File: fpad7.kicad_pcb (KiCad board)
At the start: 2 copper layers, 100 x 100 mm, 73 parts, among them J2 Conn_01x12, SW1 SW_Push, SW10 SW_Push, SW11 SW_Push, SW12 SW_Push, SW13 SW_Push, SW14 SW_Push, SW15 SW_Push, SW16 SW_Push, SW17 SW_Push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

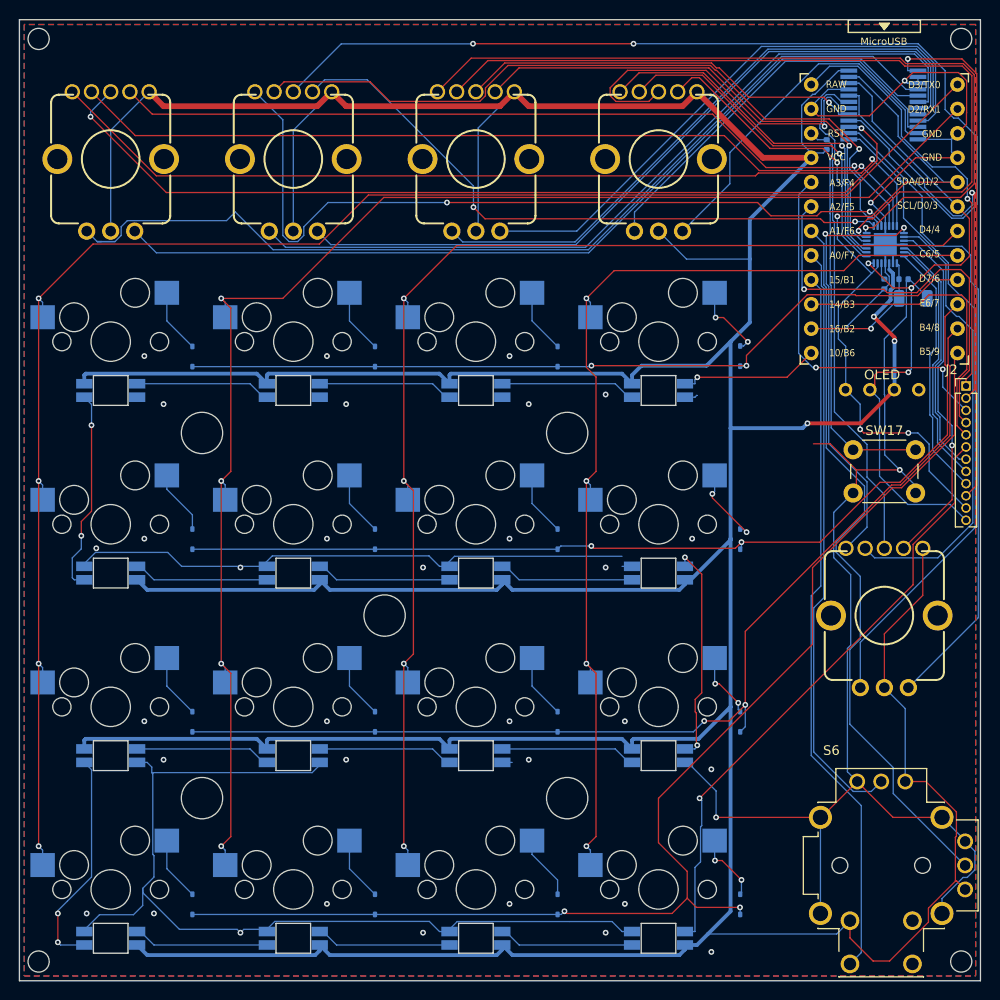
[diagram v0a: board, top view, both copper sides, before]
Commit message: update: errata for rev1
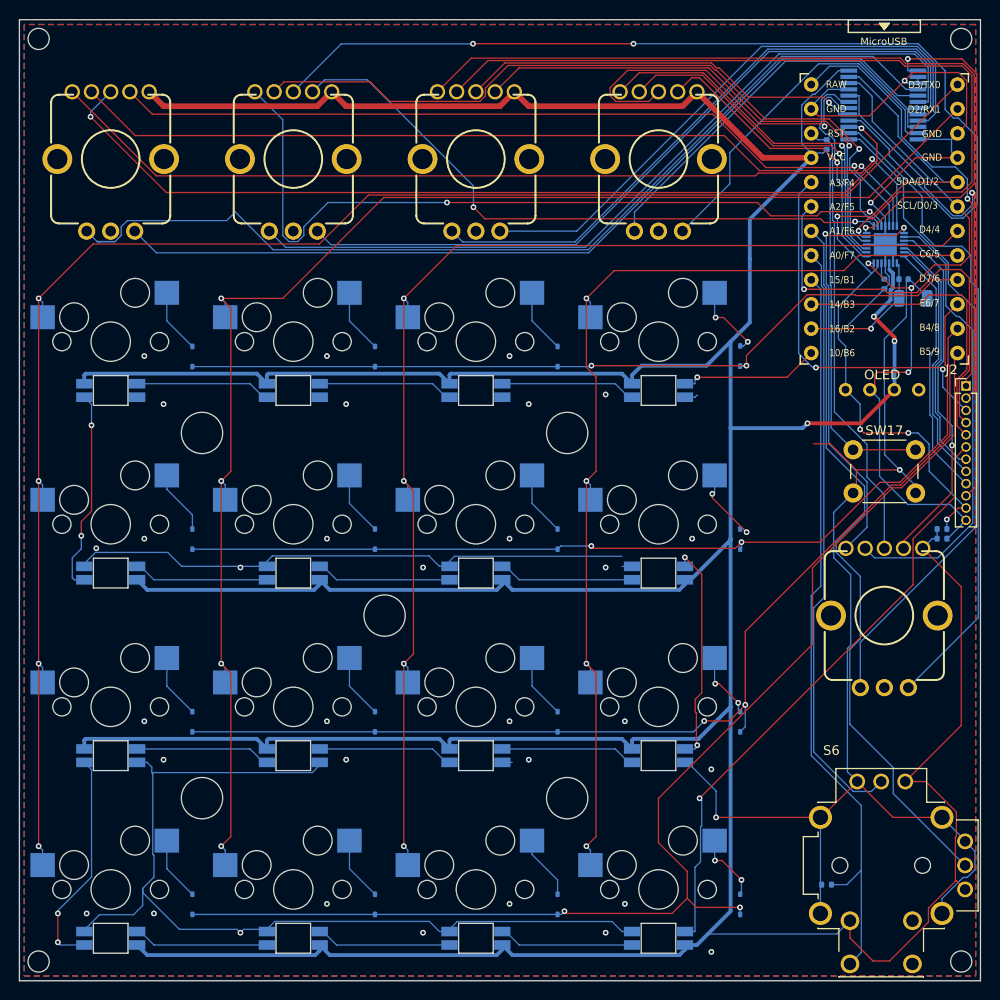
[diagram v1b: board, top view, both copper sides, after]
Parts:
- added R4: 10k, Resistor_SMD:R_0402_1005Metric, B.Cu at (104.0, 110.0)
- added R5: 3k3, Resistor_SMD:R_0402_1005Metric, B.Cu at (116.0, 73.0)
- added R6: 3k3, Resistor_SMD:R_0402_1005Metric, B.Cu at (116.0, 74.0)
- R1: value 7.6k -> 7.5k
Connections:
- S1 pad C: VCC -> GND
- S2 pad C: VCC -> GND
- S3 pad C: VCC -> GND
- S4 pad C: VCC -> GND
- S5 pad C: VCC -> GND
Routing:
- net VCC: track 621.1 -> 566.4 mm
- net /SW: track 74.7 -> 78.4 mm
- net /SDA: track 74.4 -> 77.9 mm, vias 3 -> 4
- net /SCL: track 71.9 -> 74.7 mm

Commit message: fix: rot sw should be pull down
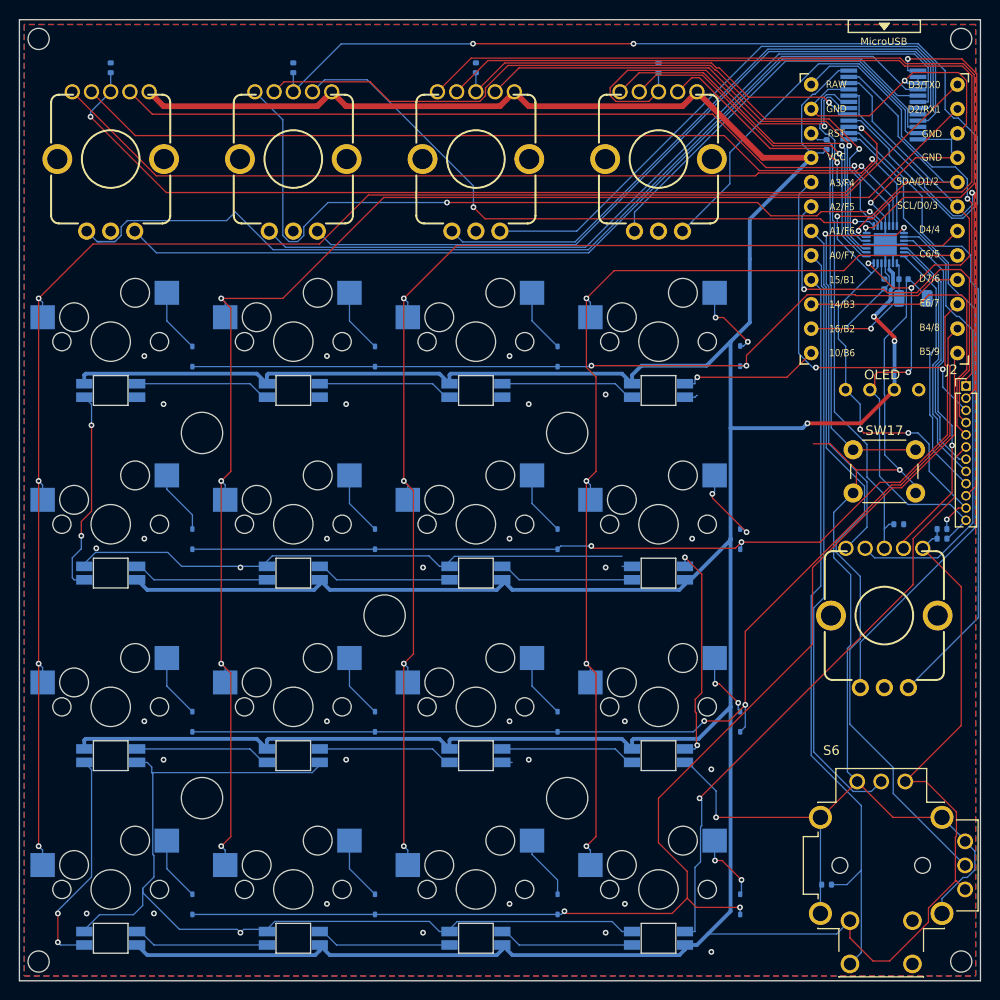
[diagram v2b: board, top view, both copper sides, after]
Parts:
- added R10: 10k, Resistor_SMD:R_0402_1005Metric, B.Cu at (86.5, 25.0)
- added R11: 10k, Resistor_SMD:R_0402_1005Metric, B.Cu at (111.5, 72.5)
- added R7: 10k, Resistor_SMD:R_0402_1005Metric, B.Cu at (29.5, 25.0)
- added R8: 10k, Resistor_SMD:R_0402_1005Metric, B.Cu at (48.5, 25.0)
- added R9: 10k, Resistor_SMD:R_0402_1005Metric, B.Cu at (67.5, 25.0)
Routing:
- net /ROT_SW4: track 38.1 -> 40.1 mm
- net /ROT_SW3: track 42.4 -> 44.4 mm
- net /ROT_SW2: track 105.1 -> 107.1 mm
- net /ROT_SW1: track 95.4 -> 97.3 mm
- net /ROT_SW5: track 53.3 -> 54.5 mm
